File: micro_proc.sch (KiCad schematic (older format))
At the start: 2 parts

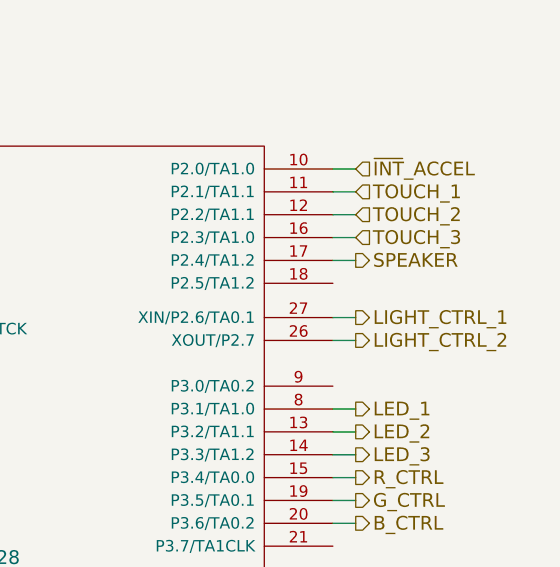
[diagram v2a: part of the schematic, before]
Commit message: added pullups/downs as necessary, added test pts
also added interrupt conn to msp from charger, made led part for generic
indicators, added generic indicators to psu's
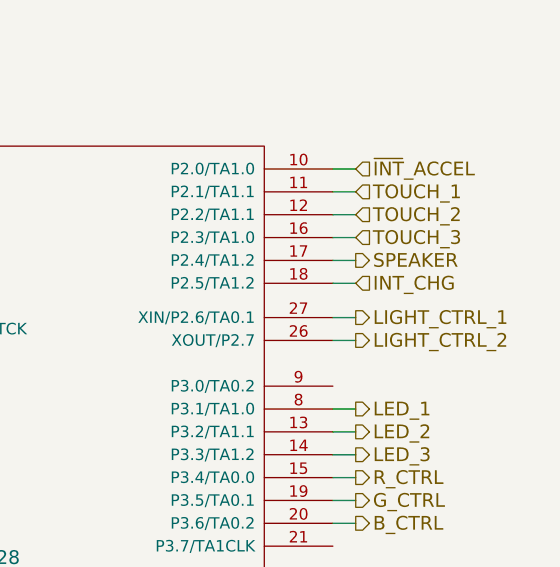
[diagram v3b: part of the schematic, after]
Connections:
- net INT_CHG: now reaches U?.18 (P2.5/TA1.2)
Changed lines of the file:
@@
 Sheet 6 18
 Title ""
-Date "14 dec 2013"
+Date "18 dec 2013"
 Rev ""
 Comp ""
@@
 Wire Wire Line
 	4100 3300 4200 3300
+Text HLabel 7900 2450 2    60   Input ~ 0
+INT_CHG
+Wire Wire Line
+	7800 2450 7900 2450
 $EndSCHEMATC

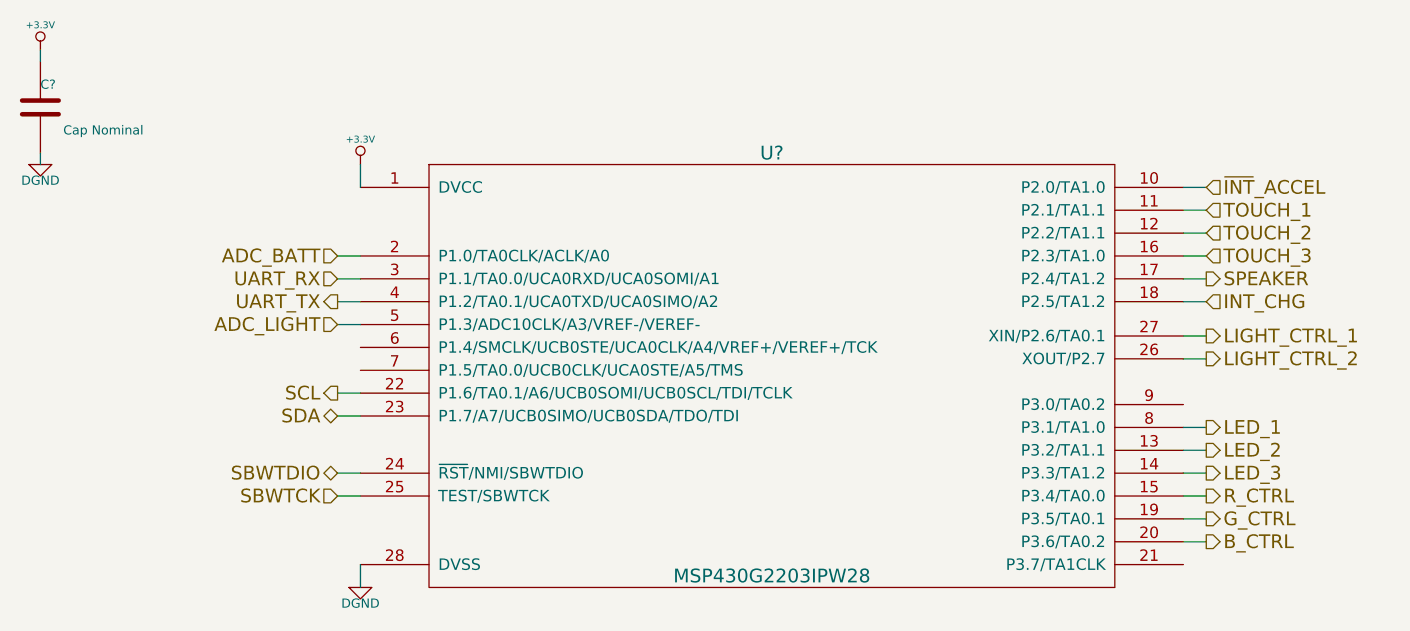
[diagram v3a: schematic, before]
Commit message: various fixes due to issues found in ERC
learned how to use invisible pins
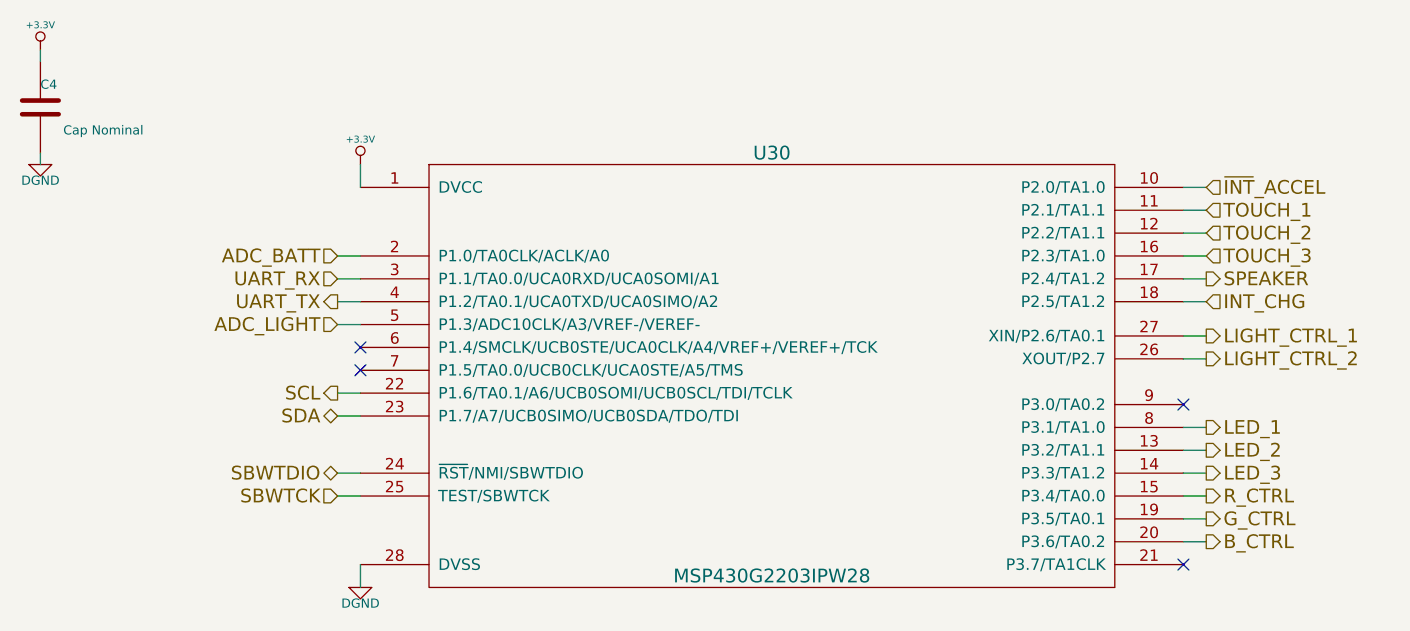
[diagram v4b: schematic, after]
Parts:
- gave numbers to parts that had none: 2
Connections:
- no-connect marks 0 -> 4
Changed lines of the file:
@@
 Sheet 6 18
 Title ""
-Date "18 dec 2013"
+Date "20 dec 2013"
 Rev ""
 Comp ""
@@
 $EndDescr
 $Comp
-L MSP430G2203IPW28 U?
+L MSP430G2203IPW28 U30
 U 1 1 529C2A65
 P 6000 1850
-F 0 "U?" H 6000 1900 60  0000 C CNN
+F 0 "U30" H 6000 1900 60  0000 C CNN
 F 1 "MSP430G2203IPW28" H 6000 50  60  0000 C CNN
 F 2 "~" H 5950 1850 60  0000 C CNN
@@
 SCL
 $Comp
-L C C?
+L C C4
 U 1 1 52A38C98
 P 2800 1600
-F 0 "C?" H 2800 1700 40  0000 L CNN
+F 0 "C4" H 2800 1700 40  0000 L CNN
 F 1 "Cap Nominal" H 2900 1500 40  0000 L CNN
 F 2 "~" H 2838 1450 30  0000 C CNN
@@
 $EndComp
 $Comp
-L +3.3V #PWR?
+L +3.3V #PWR035
 U 1 1 52A38C9E
 P 2800 1350
-F 0 "#PWR?" H 2800 1310 30  0001 C CNN
+F 0 "#PWR035" H 2800 1310 30  0001 C CNN
 F 1 "+3.3V" H 2800 1460 30  0000 C CNN
 F 2 "" H 2800 1350 60  0000 C CNN
@@
 $EndComp
 $Comp
-L DGND #PWR?
+L DGND #PWR036
 U 1 1 52A38CA4
 P 2800 1850
-F 0 "#PWR?" H 2800 1850 40  0001 C CNN
+F 0 "#PWR036" H 2800 1850 40  0001 C CNN
 F 1 "DGND" H 2800 1780 40  0000 C CNN
 F 2 "" H 2800 1850 60  0000 C CNN
@@
 	4100 2850 4200 2850
 $Comp
-L +3.3V #PWR?
+L +3.3V #PWR037
 U 1 1 52A4573A
 P 4200 1850
-F 0 "#PWR?" H 4200 1810 30  0001 C CNN
+F 0 "#PWR037" H 4200 1810 30  0001 C CNN
 F 1 "+3.3V" H 4200 1960 30  0000 C CNN
 F 2 "" H 4200 1850 60  0000 C CNN
@@
 	4200 1850 4200 1950
 $Comp
-L DGND #PWR?
+L DGND #PWR038
 U 1 1 52A45745
 P 4200 3700
-F 0 "#PWR?" H 4200 3700 40  0001 C CNN
+F 0 "#PWR038" H 4200 3700 40  0001 C CNN
 F 1 "DGND" H 4200 3630 40  0000 C CNN
 F 2 "" H 4200 3700 60  0000 C CNN
@@
 Wire Wire Line
 	7800 2450 7900 2450
+NoConn ~ 4200 2650
+NoConn ~ 4200 2750
+NoConn ~ 7800 2900
+NoConn ~ 7800 3600
 $EndSCHEMATC

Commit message: placed components ... quite the task!
there is a lot of shit going on in this board... :D
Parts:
- renumbered C4 to C3
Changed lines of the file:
@@
 $Descr A4 11693 8268
 encoding utf-8
-Sheet 6 18
+Sheet 6 15
 Title ""
-Date "12 jan 2014"
+Date "18 jan 2014"
 Rev ""
 Comp ""
@@
 SCL
 $Comp
-L C C4
+L C C3
 U 1 1 52A38C98
 P 2800 1600
-F 0 "C4" H 2800 1700 40  0000 L CNN
+F 0 "C3" H 2800 1700 40  0000 L CNN
 F 1 "Cap Nominal" H 2900 1500 40  0000 L CNN
 F 2 "~" H 2838 1450 30  0000 C CNN
@@
 $EndComp
 $Comp
-L +3.3V #PWR035
+L +3.3V #PWR033
 U 1 1 52A38C9E
 P 2800 1350
-F 0 "#PWR035" H 2800 1310 30  0001 C CNN
+F 0 "#PWR033" H 2800 1310 30  0001 C CNN
 F 1 "+3.3V" H 2800 1460 30  0000 C CNN
 F 2 "" H 2800 1350 60  0000 C CNN
@@
 $EndComp
 $Comp
-L DGND #PWR036
+L DGND #PWR034
 U 1 1 52A38CA4
 P 2800 1850
-F 0 "#PWR036" H 2800 1850 40  0001 C CNN
+F 0 "#PWR034" H 2800 1850 40  0001 C CNN
 F 1 "DGND" H 2800 1780 40  0000 C CNN
 F 2 "" H 2800 1850 60  0000 C CNN
@@
 	4100 2850 4200 2850
 $Comp
-L +3.3V #PWR037
+L +3.3V #PWR035
 U 1 1 52A4573A
 P 4200 1850
-F 0 "#PWR037" H 4200 1810 30  0001 C CNN
+F 0 "#PWR035" H 4200 1810 30  0001 C CNN
 F 1 "+3.3V" H 4200 1960 30  0000 C CNN
 F 2 "" H 4200 1850 60  0000 C CNN
@@
 	4200 1850 4200 1950
 $Comp
-L DGND #PWR038
+L DGND #PWR036
 U 1 1 52A45745
 P 4200 3700
-F 0 "#PWR038" H 4200 3700 40  0001 C CNN
+F 0 "#PWR036" H 4200 3700 40  0001 C CNN
 F 1 "DGND" H 4200 3630 40  0000 C CNN
 F 2 "" H 4200 3700 60  0000 C CNN
